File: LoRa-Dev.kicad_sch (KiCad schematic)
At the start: 19 parts, among them J1 Conn_Coaxial_Small, J2 Barrel_Jack_MountingPin, U1 RPi Pico, U2 LT1963AEQ, U3 LoRa126XF30

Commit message: Fixed minor layout issues
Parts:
- removed C3: 47uF, Capacitor_SMD:CP_Elec_6.3x5.8, symbol Device:C_Polarized_Small
- added C3: 47uF, Capacitor_SMD:C_1210_3225Metric, symbol Device:C_Small
- R9: value R_Small -> 0R
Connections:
- net GND: now also C3.2
- net RF_VDD: now also C3.1
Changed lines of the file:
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@@
 			)
 		)
-		(property "Value" "R_Small"
+		(property "Value" "0R"
 			(at 226.06 69.85 90)
 			(effects
@@
 	)
 	(symbol
-		(lib_id "Device:C_Polarized_Small")
-		(at 143.51 71.12 0)
-		(unit 1)
-		(exclude_from_sim no)
-		(in_bom yes)
-		(on_board yes)
-		(dnp no)
-		(fields_autoplaced yes)
-		(property "Reference" "C3"
-			(at 146.05 69.3038 0)
-			(effects
-				(font
-					(size 1.27 1.27)
-				)
-				(justify left)
-			)
-		)
-		(property "Value" "47uF"
-			(at 146.05 71.8438 0)
-			(effects
-				(font
-					(size 1.27 1.27)
-				)
-				(justify left)
-			)
-		)
-		(property "Footprint" "Capacitor_SMD:CP_Elec_6.3x5.8"
-			(at 143.51 71.12 0)
-			(effects
-				(font
-					(size 1.27 1.27)
-				)
-				(hide yes)
-			)
-		)
-		(property "Datasheet" "~"
-			(at 143.51 71.12 0)
-			(effects
-				(font
-					(size 1.27 1.27)
-				)
-				(hide yes)
-			)
-		)
-		(property "Description" "Polarized capacitor, small symbol"
-			(at 143.51 71.12 0)
-			(effects
-				(font
-					(size 1.27 1.27)
-				)
-				(hide yes)
-			)
-		)
-		(pin "1"
-		)
-		(pin "2"
-		)
-		(instances
-			(project ""
-				(path "/ef1cdc4e-4ca4-4643-8589-6d5225afae9e"
-					(reference "C3")
-					(unit 1)
-				)
-			)
-		)
-	)
-	(symbol
 		(lib_id "Device:R_Small")
 		(at 66.04 125.73 90)
@@
 					(unit 1)
 				)
+			)
+		)
+	)
+	(symbol
+		(lib_id "Device:C_Small")
+		(at 143.51 71.12 0)
+		(unit 1)
+		(exclude_from_sim no)
+		(in_bom yes)
+		(on_board yes)
+		(dnp no)
+		(fields_autoplaced yes)
+		(property "Reference" "C3"
+			(at 146.05 69.8562 0)
+			(effects
+				(font
+					(size 1.27 1.27)
+				)
+				(justify left)
+			)
+		)
+		(property "Value" "47uF"
+			(at 146.05 72.3962 0)
+			(effects
+				(font
+					(size 1.27 1.27)
+				)
+				(justify left)
+			)
+		)
+		(property "Footprint" "Capacitor_SMD:C_1210_3225Metric"
+			(at 143.51 71.12 0)
+			(effects
+				(font
+					(size 1.27 1.27)
+				)
+				(hide yes)
+			)
+		)
+		(property "Datasheet" "~"
+			(at 143.51 71.12 0)
+			(effects
+				(font
+					(size 1.27 1.27)
+				)
+				(hide yes)
+			)
+		)
+		(property "Description" "Unpolarized capacitor, small symbol"
+			(at 143.51 71.12 0)
+			(effects
+				(font
+					(size 1.27 1.27)
+				)
+				(hide yes)
+			)
+		)
+		(pin "2"
+		)
+		(pin "1"
+		)
+		(instances
+			(project "LoRa-Dev"
+				(path "/ef1cdc4e-4ca4-4643-8589-6d5225afae9e"
+					(reference "C3")
+					(unit 1)
+				)

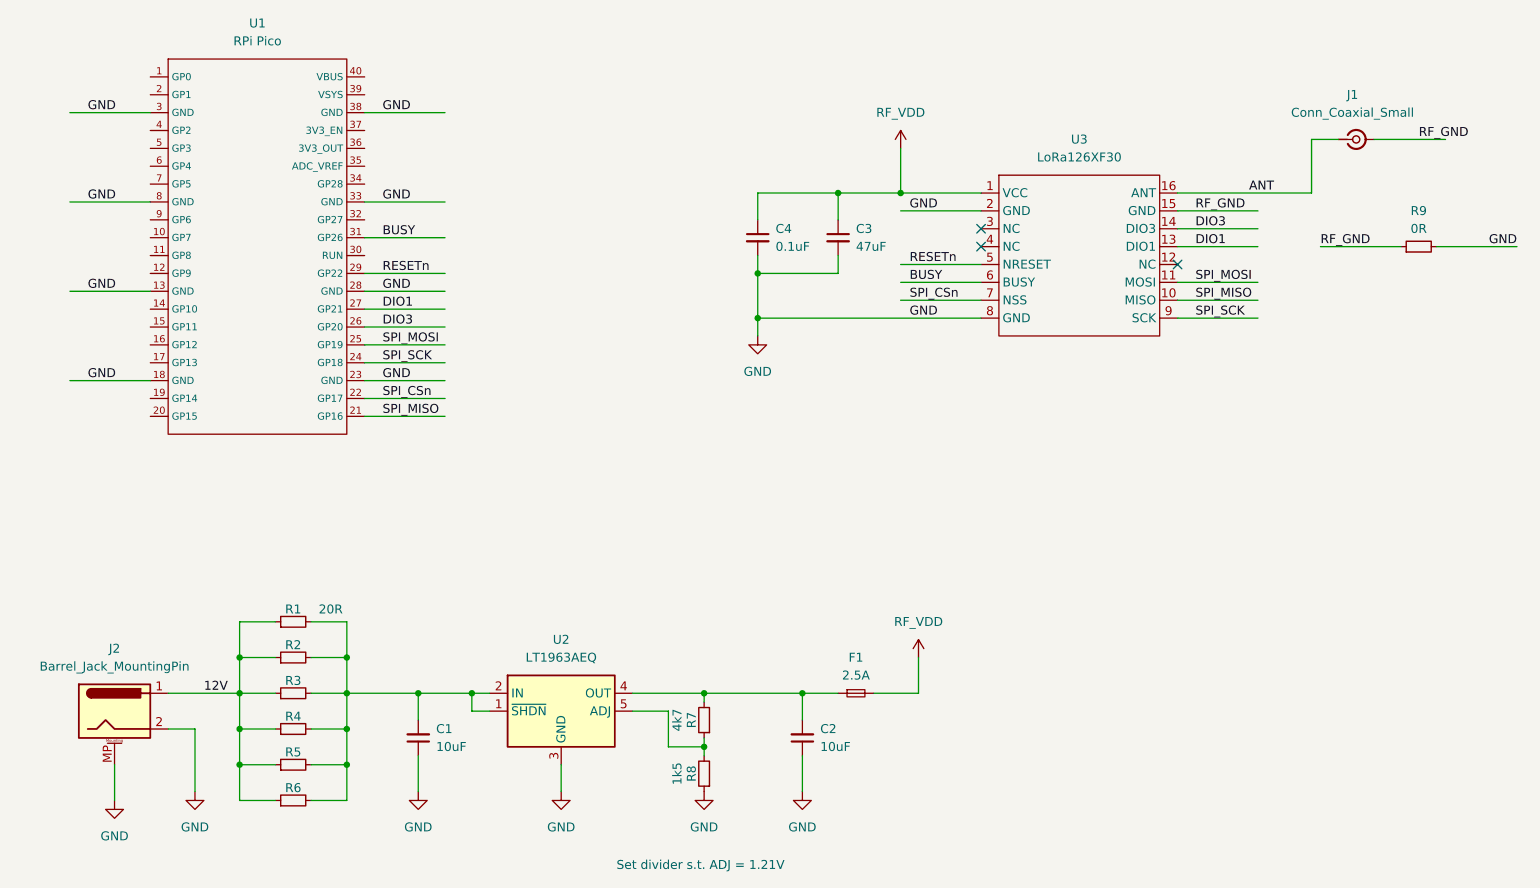
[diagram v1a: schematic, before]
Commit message: Minor fixes, exported BOM
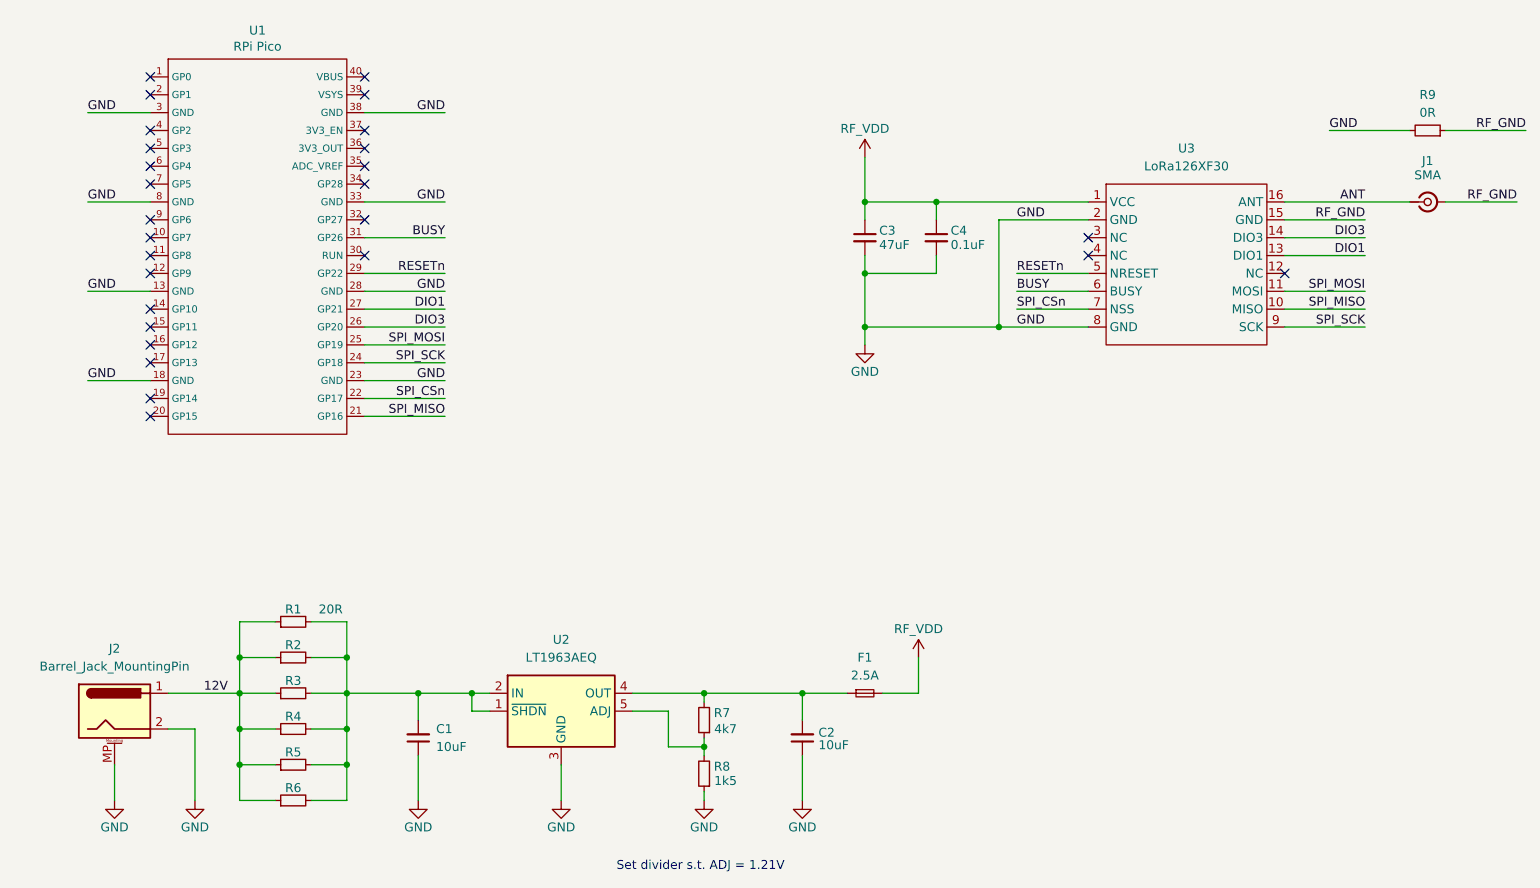
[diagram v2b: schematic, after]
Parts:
- J1: value Conn_Coaxial_Small -> SMA; footprint Connector_Coaxial:U.FL_Hirose_U.FL-R-SMT-1_Vertical -> Connector_Coaxial:SMA_Amphenol_901-144_Vertical
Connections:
- no-connect marks 3 -> 27
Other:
- moved on the sheet: C3, C4, F1, J1, R9, U3
